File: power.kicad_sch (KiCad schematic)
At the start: 10 parts, among them J17 Conn_01x04_Socket, U24 LM3940IMPX-3.3/NOPB, U27 LM2940IMPX-12/NOPB

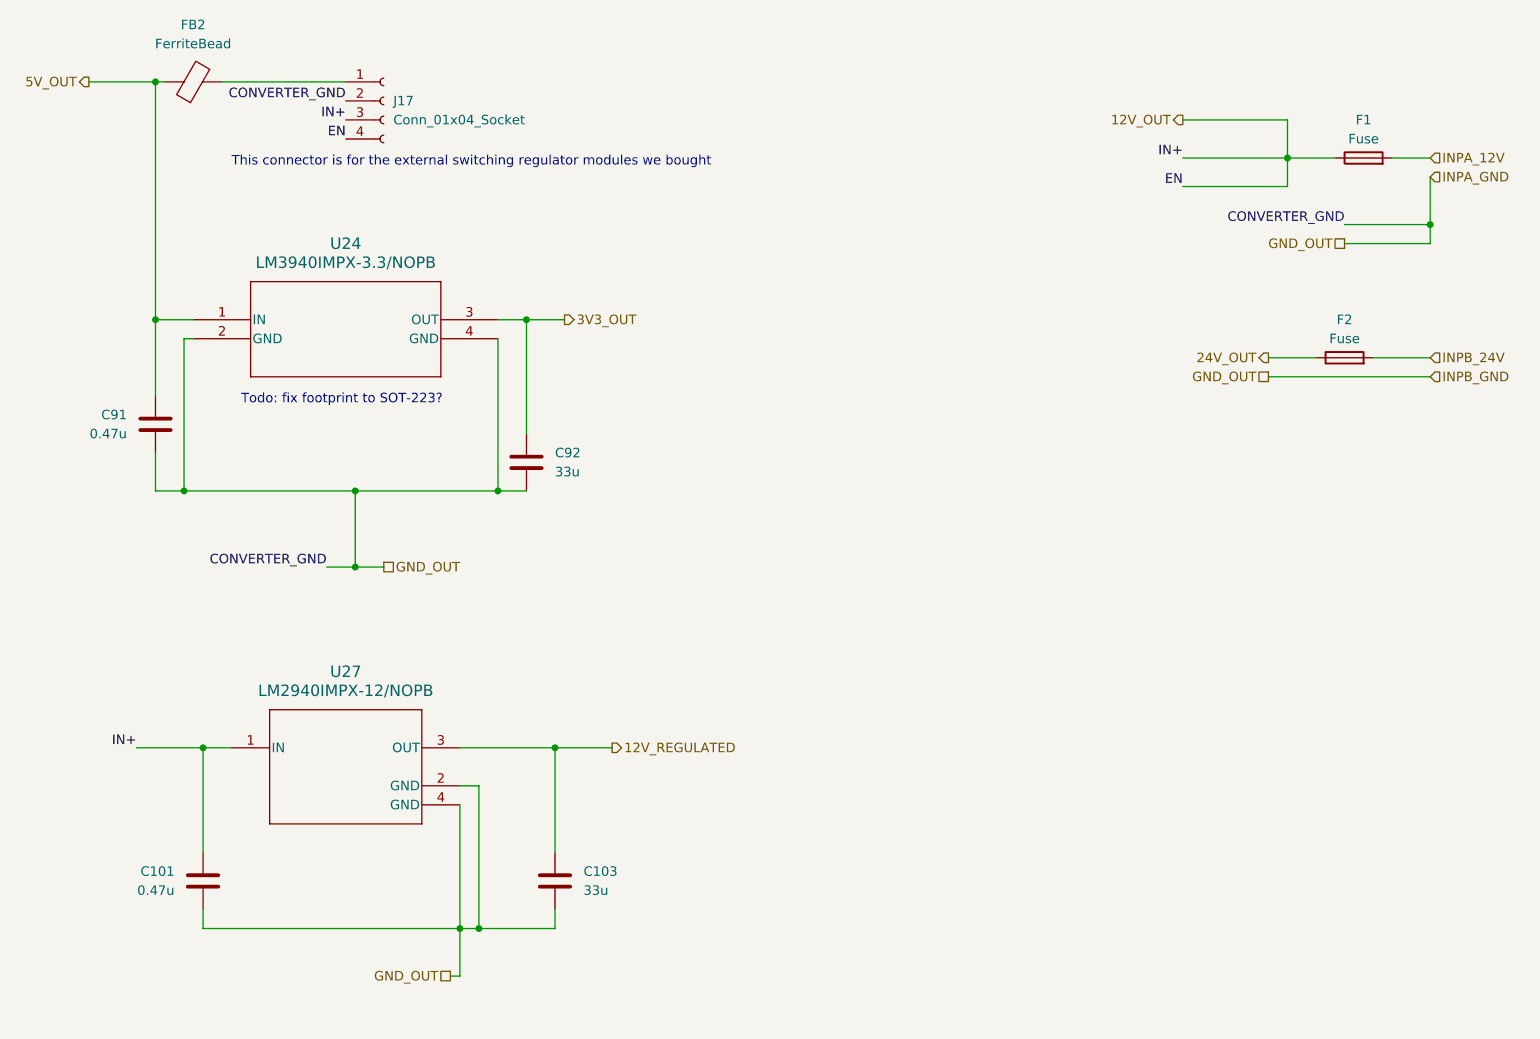
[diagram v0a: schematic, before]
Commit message: added footprints to almost all components
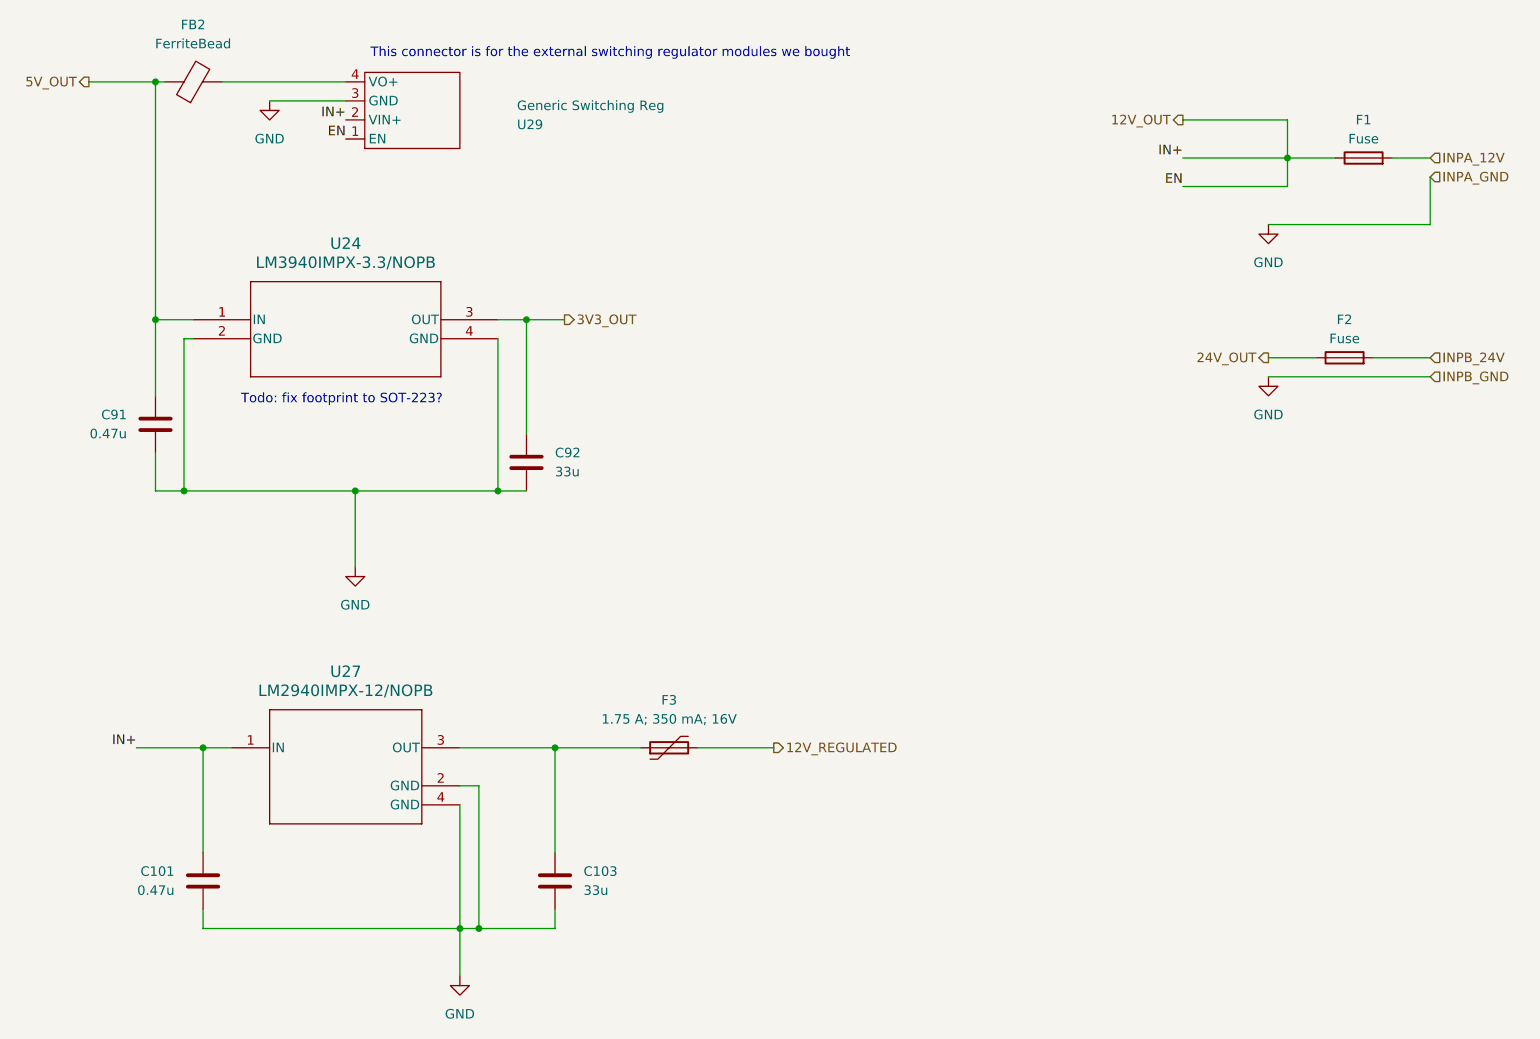
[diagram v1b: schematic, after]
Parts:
- removed J17: Conn_01x04_Socket, symbol Connector:Conn_01x04_Socket
- added F3: 1.75 A; 350 mA; 16V, Fuse:Fuse_0805_2012Metric_Pad1.15x1.40mm_HandSolder, symbol Device:Polyfuse
- added U29: Generic Switching Reg, symbol LaunchpadControllerLib:GenericSwitchingReg
- C101, C103, C91, C92: footprint (none) -> Capacitor_SMD:C_0603_1608Metric_Pad1.08x0.95mm_HandSolder
- F1, F2: footprint (none) -> Fuse:Fuse_Keystone_3557-2; Mouser# (none) -> 534-3557-2
- FB2: footprint (none) -> Inductor_SMD:L_0805_2012Metric_Pad1.15x1.40mm_HandSolder; Mouser# (none) -> 81-BLM18KG102SN1D
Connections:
- net 12V_OUT: now also U29.1 (EN), U29.2 (VIN+)
- net 12V_REGULATED: now also F3.2; no longer C103.1, U27.3 (OUT)
- net at FB2.2: now also U29.4 (VO+)
- net GND_OUT renamed GND
- net GND: now also U29.3 (GND)
- new net: C103.1, F3.1, U27.3 (OUT)
